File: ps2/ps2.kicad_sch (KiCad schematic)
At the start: 28 parts, among them J1 keyboard, J2 perslot1a, J3 perslot1b, Q1 Q_NPN_CBE, Q2 Q_PNP_EBC, U1 74HC74, U10 74HC280, U11 74HC541, U2 74HC08, U3 74HC14, U4 74HC05, U5 74HC688, U6 74HC195, U7 74HC195, U8 74HC195, U9 74HC541

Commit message: applied sf68 & ps2 fixes stash from master
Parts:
- R7: value 20k -> 4k7
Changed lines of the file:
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@@
 			)
 		)
-		(property "Value" "20k"
+		(property "Value" "4k7"
 			(at 187.96 68.58 90)
 			(effects

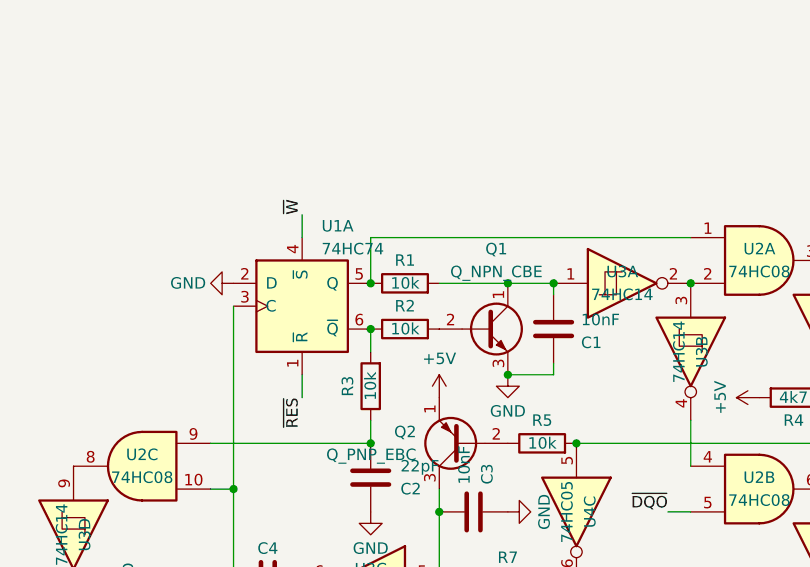
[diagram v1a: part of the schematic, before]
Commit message: [ps2] fixed send request RC constant 	t must be >= 100us 	RC was being t, therefore t was actually smaller than 100us 	RC is now >= 1.28 * 100us (R : 10kohm -> 14.7kohm) 	t ~= 120us >= 100us
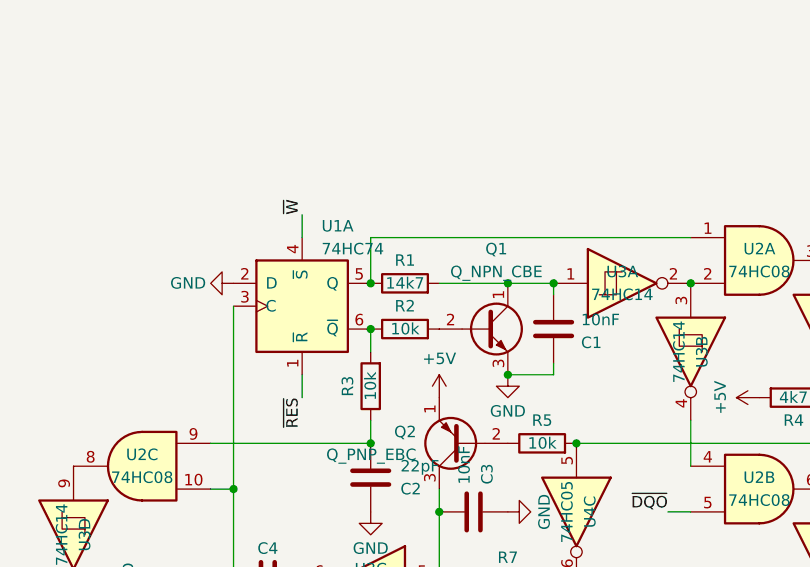
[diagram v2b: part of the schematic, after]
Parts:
- R1: value 10k -> 14k7
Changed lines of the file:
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@@
 			)
 		)
-		(property "Value" "10k"
+		(property "Value" "14k7"
 			(at 176.53 35.56 90)
 			(effects

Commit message: lcd2x16 ready
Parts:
- removed C1, C3: 10nF, Capacitor_THT:C_Disc_D3.0mm_W1.6mm_P2.54mm, symbol Device:C
- removed C2, C4: 22pF, Capacitor_THT:C_Disc_D3.0mm_W1.6mm_P2.54mm, symbol Device:C
- removed Q1: Q_NPN_CBE, Package_TO_SOT_THT:TO-92, symbol Transistor_BJT:Q_NPN_CBE
- removed Q2: Q_PNP_EBC, Package_TO_SOT_THT:TO-92, symbol Transistor_BJT:Q_PNP_EBC
- removed R1: 14k7, Resistor_THT:R_Axial_DIN0207_L6.3mm_D2.5mm_P2.54mm_Vertical, symbol Device:R
- removed R2, R3, R5, R6: 10k, Resistor_THT:R_Axial_DIN0207_L6.3mm_D2.5mm_P2.54mm_Vertical, symbol Device:R
- removed R4, R7, R8: 4k7, Resistor_THT:R_Axial_DIN0207_L6.3mm_D2.5mm_P2.54mm_Vertical, symbol Device:R
- removed unit 2 of U1
- removed unit 1 of U1
- removed U10: 74HC280, Package_DIP:DIP-14_W7.62mm, symbol 74xx:74LS280
- removed U11: 74HC541, Package_DIP:DIP-20_W7.62mm, symbol 74xx:74LS541
- removed U2: 74HC08, Package_DIP:DIP-14_W7.62mm, symbol 74xx:74LS08
- removed U3: 74HC14, Package_DIP:DIP-14_W7.62mm, symbol 74xx:74HC14
- removed U4: 74HC05, Package_DIP:DIP-14_W7.62mm, symbol 74xx:74LS05
- removed U6, U7, U8: 74HC195, Package_DIP:DIP-16_W7.62mm, symbol 74xx:74LS195
- added J3: port1, Connector_TE-Connectivity:57492651, symbol Connector:Mini-DIN-6
- added U3: 74HC32, Package_DIP:DIP-14_W7.62mm, symbol 74xx:74LS32
- J2: renamed from J1; value keyboard -> port0
- renumbered J2 to J1, J3 to J4, U5 to U2, U9 to U4
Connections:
- net +5V: now also J3.4
- net A_{1}: no longer U2.17 (P7)
- net A_{2}: now also U2.2 (P0); no longer U2.15 (P6)
- net A_{3}: now also U2.4 (P1); no longer U2.13 (P5)
- net A_{4}: now also U2.6 (P2); no longer U2.11 (P4)
- net A_{6}: now also U2.11 (P4); no longer U2.6 (P2)
- net A_{7}: now also U2.13 (P5); no longer U2.4 (P1)
- net BE.~{IO}: now also U2.17 (P7); no longer U2.2 (P0)
- net GND: now also U2.15 (P6), J3.3; no longer U4.8 (A6)
- net ~{S}: now also U3.13
- net ~{W}: now also U3.11
- net DIR.~{W}: now reaches J1.7 (Pin_7)
- net DIR.~{W}: now also U3.12
- net DAT renamed DAT_{0}
- net ~{CLK} renamed ~{CLK_{0}}
- new net DAT_{1}: J3.1
- new net PORT: U4.8 (A6)
- new net ~{CLK_{1}}: J3.5
- no-connect marks 55 -> 44
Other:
- added sheet controller (controller.kicad_sch)
- added sheet ports_mux (ports_mux.kicad_sch)
- added sheet shift_registers (shift_registers.kicad_sch)
- note added: "IO port 00h/01h <="
- note added: "irq 01h/03h, pri. 2/3"
- note removed: "IO port 00h <="
- note removed: "irq 01h, pri. 2/3"
- note removed: "ugly OR (/W = /DIR.W + /S)"
- moved on the sheet: J2, U4

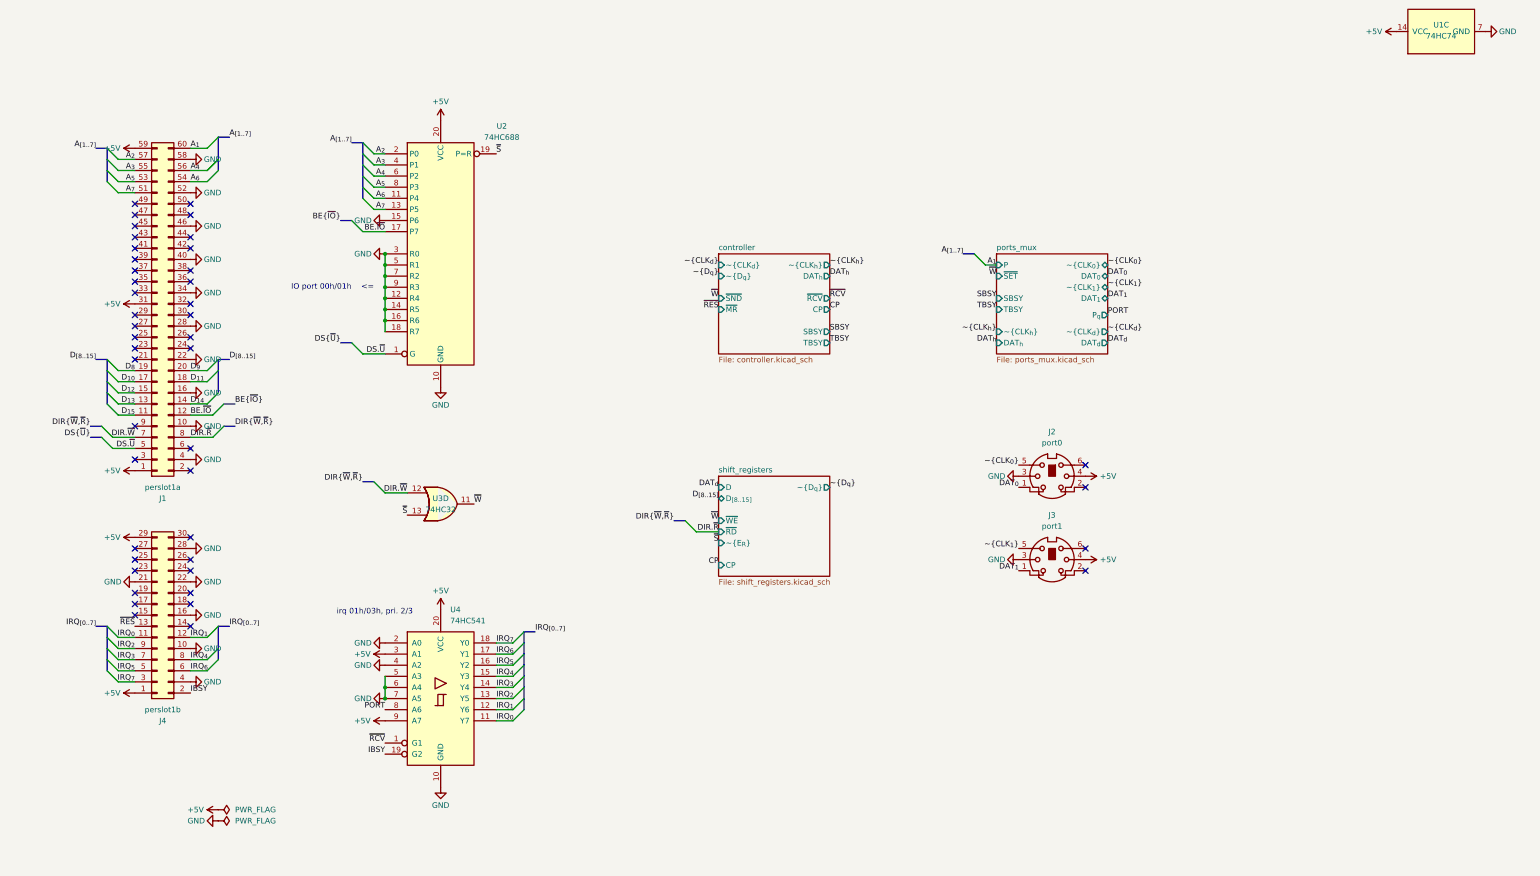
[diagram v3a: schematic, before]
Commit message: [ps2]:	made pcb design of the new latest schematic
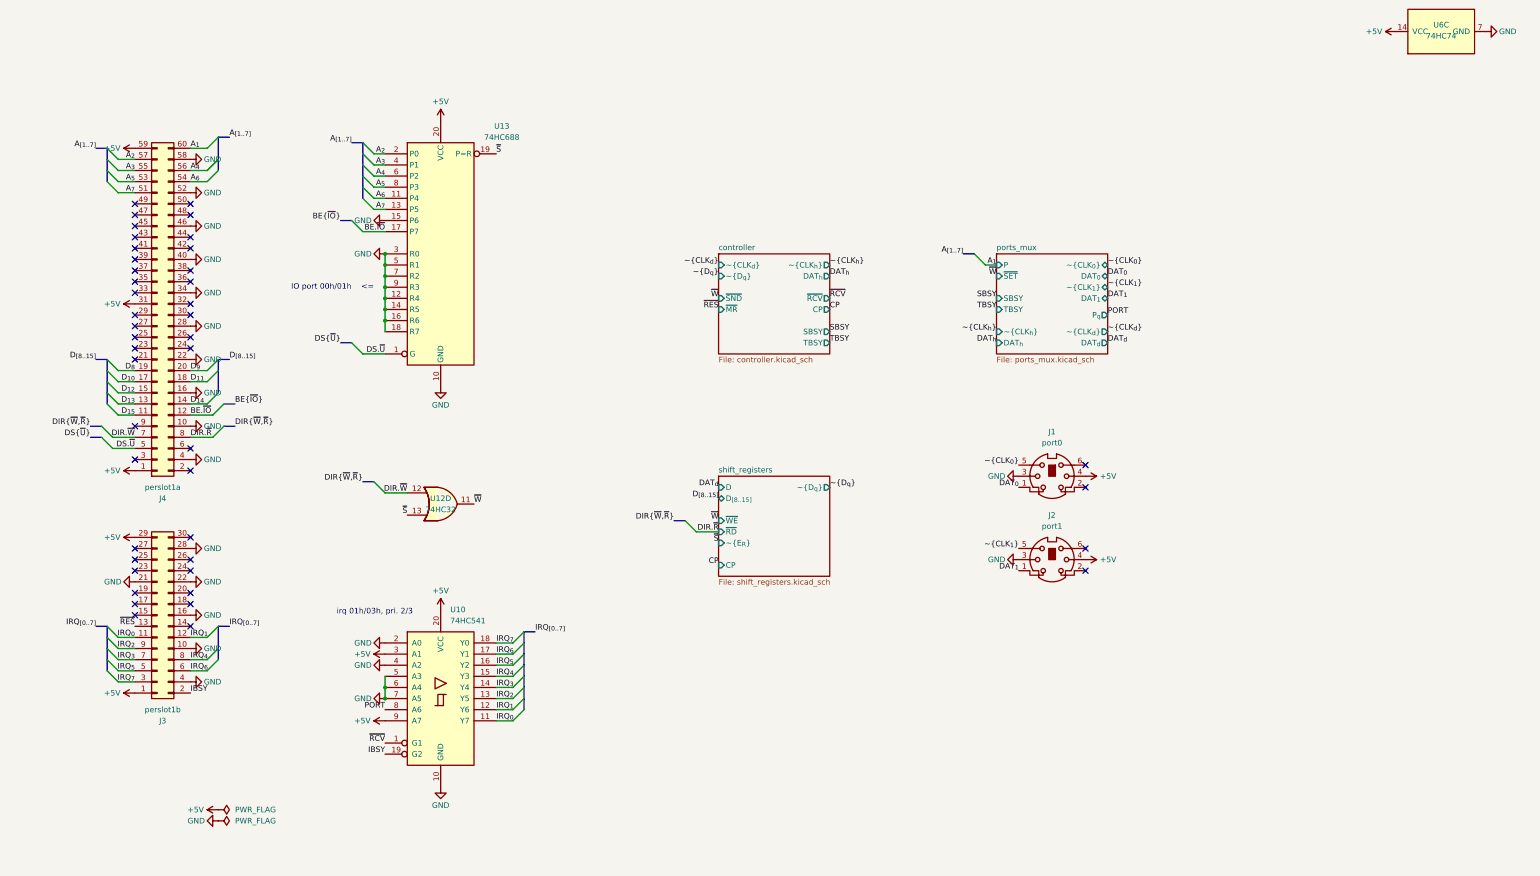
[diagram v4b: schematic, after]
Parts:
- renumbered J2 to J1, J3 to J2, J4 to J3, J1 to J4, U4 to U10, U3 to U12, U2 to U13, U1 to U6
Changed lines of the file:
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@@
 		(on_board yes)
 		(dnp no)
-		(property "Reference" "U3"
+		(property "Reference" "U12"
 			(at 101.6 106.68 0)
 			(effects
@@
 			)
 		)
-		(property "Datasheet" "http://www.ti.com/lit/gpn/sn74LS32"
+		(property "Datasheet" ""
 			(at 101.6 107.95 0)
 			(effects
@@
 			)
 		)
-		(property "Description" "Quad 2-input OR"
+		(property "Description" ""
 			(at 101.6 107.95 0)
 			(effects
@@
 			(project "ps2"
 				(path "/0417edbf-d6ac-46fa-bfd1-1542e1b615ef"
-					(reference "U3")
+					(reference "U12")
 					(unit 4)
 				)
@@
 		(on_board yes)
 		(dnp no)
-		(property "Reference" "J4"
+		(property "Reference" "J3"
 			(at 38.1 157.48 0)
 			(effects
@@
 			(project "ps2"
 				(path "/0417edbf-d6ac-46fa-bfd1-1542e1b615ef"
-					(reference "J4")
+					(reference "J3")
 					(unit 1)
 				)
@@
 		(on_board yes)
 		(dnp no)
-		(property "Reference" "J1"
+		(property "Reference" "J4"
 			(at 38.1 106.68 0)
 			(effects
@@
 			(project "ps2"
 				(path "/0417edbf-d6ac-46fa-bfd1-1542e1b615ef"
-					(reference "J1")
+					(reference "J4")
 					(unit 1)
 				)
@@
 		(dnp no)
 		(fields_autoplaced yes)
-		(property "Reference" "U4"
+		(property "Reference" "U10"
 			(at 103.7941 132.08 0)
 			(effects
@@
 			)
 		)
-		(property "Datasheet" "http://www.ti.com/lit/gpn/sn74LS541"
+		(property "Datasheet" ""
 			(at 101.6 152.4 0)
 			(effects
@@
 			)
 		)
-		(property "Description" "8-bit Buffer/Line Driver 3-state outputs"
+		(property "Description" ""
 			(at 101.6 152.4 0)
 			(effects
@@
 			(project "ps2"
 				(path "/0417edbf-d6ac-46fa-bfd1-1542e1b615ef"
-					(reference "U4")
+					(reference "U10")
 					(unit 1)
 				)
@@
 		(on_board yes)
 		(dnp no)
-		(property "Reference" "U1"
+		(property "Reference" "U6"
 			(at 330.2 -1.524 90)
 			(effects
@@
 			)
 		)
-		(property "Datasheet" "74xx/74hc_hct74.pdf"
+		(property "Datasheet" ""
 			(at 330.2 0 0)
 			(effects
@@
 			)
 		)
-		(property "Description" "Dual D Flip-flop, Set & Reset"
+		(property "Description" ""
 			(at 330.2 0 0)
 			(effects
@@
 			(project ""
 				(path "/0417edbf-d6ac-46fa-bfd1-1542e1b615ef"
-					(reference "U1")
+					(reference "U6")
 					(unit 3)
 				)
@@
 		(on_board yes)
 		(dnp no)
-		(property "Reference" "J2"
+		(property "Reference" "J1"
 			(at 241.2823 91.44 0)
 			(effects
@@
 			)
 		)
-		(property "Datasheet" "http://service.powerdynamics.com/ec/Catalog17/Section%2011.pdf"
+		(property "Datasheet" ""
 			(at 241.3 101.6 0)
 			(effects
@@
 			)
 		)
-		(property "Description" "6-pin Mini-DIN connector"
+		(property "Description" ""
 			(at 241.3 101.6 0)
 			(effects
@@
 			(project "ps2"
 				(path "/0417edbf-d6ac-46fa-bfd1-1542e1b615ef"
-					(reference "J2")
+					(reference "J1")
 					(unit 1)
 				)
@@
 		(on_board yes)
 		(dnp no)
-		(property "Reference" "J3"
+		(property "Reference" "J2"
 			(at 241.2823 110.49 0)
 			(effects
@@
 			)
 		)
-		(property "Datasheet" "http://service.powerdynamics.com/ec/Catalog17/Section%2011.pdf"
+		(property "Datasheet" ""
 			(at 241.3 120.65 0)
 			(effects
@@
 			)
 		)
-		(property "Description" "6-pin Mini-DIN connector"
+		(property "Description" ""
 			(at 241.3 120.65 0)
 			(effects
@@
 			(project "ps2"
 				(path "/0417edbf-d6ac-46fa-bfd1-1542e1b615ef"
-					(reference "J3")
+					(reference "J2")
 					(unit 1)
 				)
@@
 		(dnp no)
 		(fields_autoplaced yes)
-		(property "Reference" "U2"
+		(property "Reference" "U13"
 			(at 115.57 21.6214 0)
 			(effects
@@
 			)
 		)
-		(property "Datasheet" "https://www.ti.com/lit/ds/symlink/cd54hc688.pdf"
+		(property "Datasheet" ""
 			(at 101.6 50.8 0)
 			(effects
@@
 			)
 		)
-		(property "Description" "8-bit magnitude comparator"
+		(property "Description" ""
 			(at 101.6 50.8 0)
 			(effects
@@
 			(project "ps2"
 				(path "/0417edbf-d6ac-46fa-bfd1-1542e1b615ef"
-					(reference "U2")
+					(reference "U13")
 					(unit 1)
 				)

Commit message: [ps2]	changed fingers footprints
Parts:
- J3: footprint Connector_PCBEdge:pcb_edge_30_P2.54_new -> Connector_PCBEdge:edge_connector_15p_2.54mm
- J4: footprint Connector_PCBEdge:pcb_edge_60_P2.54_new -> Connector_PCBEdge:edge_connector_30p_2.54mm
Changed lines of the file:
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@@
 			)
 		)
-		(property "Footprint" "Connector_PCBEdge:pcb_edge_30_P2.54_new"
+		(property "Footprint" "Connector_PCBEdge:edge_connector_15p_2.54mm"
 			(at 36.83 133.35 0)
 			(effects
@@
 			)
 		)
-		(property "Footprint" "Connector_PCBEdge:pcb_edge_60_P2.54_new"
+		(property "Footprint" "Connector_PCBEdge:edge_connector_30p_2.54mm"
 			(at 36.83 64.77 0)
 			(effects
